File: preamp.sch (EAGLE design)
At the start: 30 parts, among them IC1 INA2141U, IC2 INA2141U, IC3 INA2141U

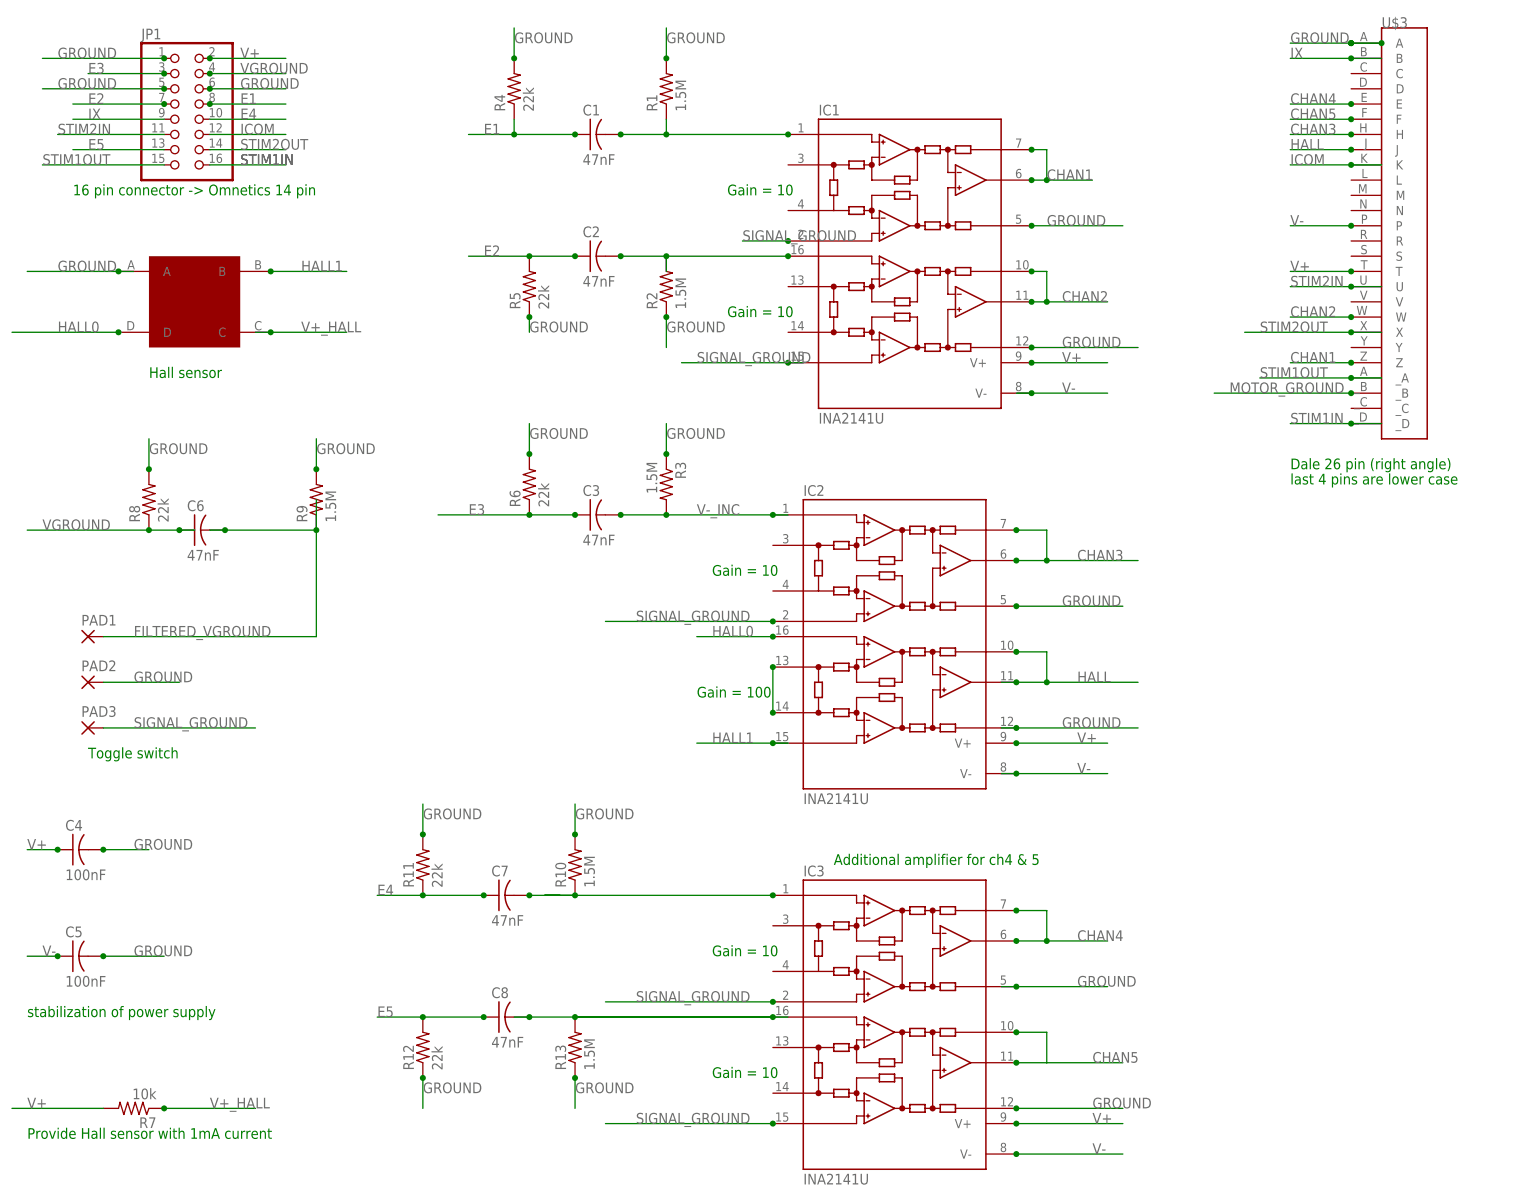
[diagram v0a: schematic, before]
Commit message: Preamp - Removed VGROUND
SIGNAL_GROUND net changed to GROUND
Removed filter circuitry for VGROUND
Removed toggle switch between GROUND and FILTERED_VGND for
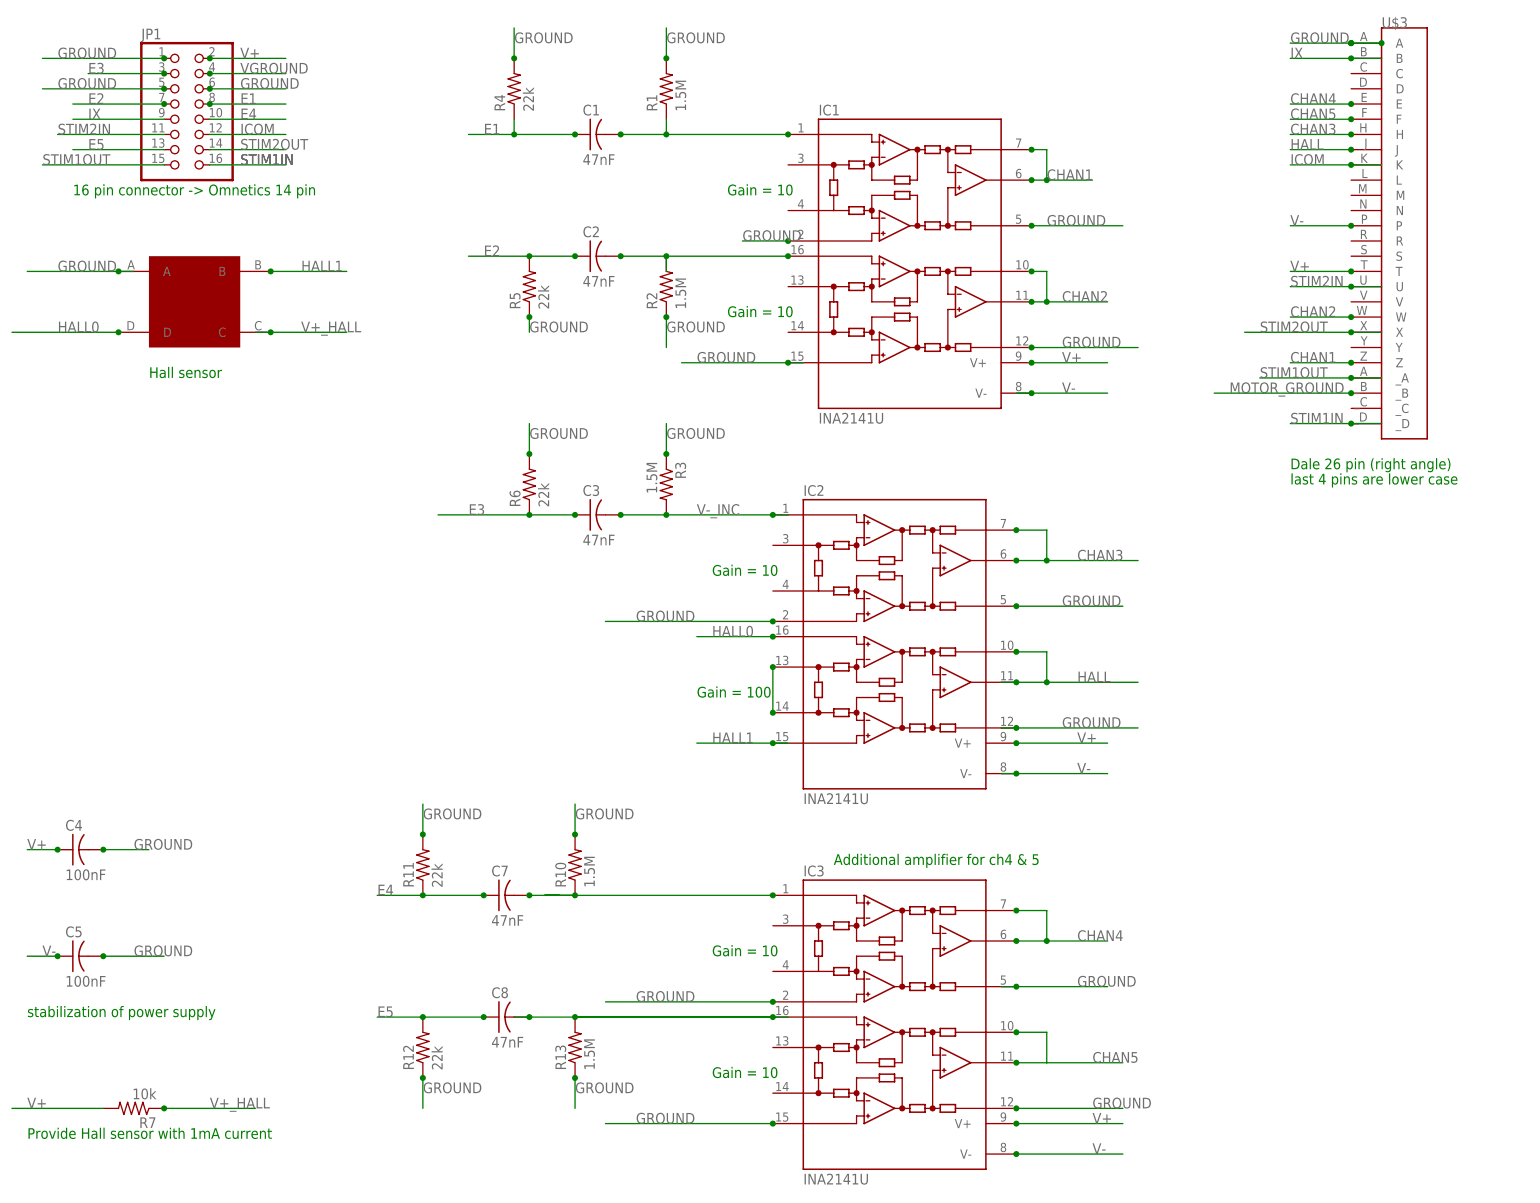
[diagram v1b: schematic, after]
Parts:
- removed C6: 47nF, elm:C0805ELM
- removed PAD1, PAD2, PAD3: (no value), wirepad:SMD2
- removed R8: 22k, elm:R0805ELM
- removed R9: 1.5M, elm:R0805ELM
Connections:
- removed net FILTERED_VGROUND: C6.2, PAD1.P, R9.1
- removed net SIGNAL_GROUND: IC1.INA+, IC1.INB+, IC2.INA+, IC3.INA+, IC3.INB+, PAD3.P
- net GROUND: now also IC1.INA+, IC1.INB+, IC2.INA+, IC3.INA+, IC3.INB+; no longer PAD2.P, R8.2, R9.2
- net VGROUND: no longer C6.1, R8.1
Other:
- note removed: "Toggle switch"
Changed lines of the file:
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@@
 <?xml version="1.0" encoding="utf-8"?>
 <!DOCTYPE eagle SYSTEM "eagle.dtd">
-<eagle version="6.2">
+<eagle version="7.5.0">
 <drawing>
 <settings>
@@
 <part name="C4" library="elm" deviceset="C0805ELM" device="" value="100nF"/>
 <part name="C5" library="elm" deviceset="C0805ELM" device="" value="100nF"/>
-<part name="R8" library="elm" deviceset="R0805ELM" device="" value="22k"/>
-<part name="C6" library="elm" deviceset="C0805ELM" device="" value="47nF"/>
-<part name="R9" library="elm" deviceset="R0805ELM" device="" value="1.5M"/>
 <part name="U$3" library="elm" deviceset="MMD1P22G-26-M101" device=""/>
 <part name="JP1" library="pinhead" deviceset="PINHD-2X8" device=""/>
 <part name="U$2" library="elm" deviceset="HALL_ON_SIDE" device="" value="HALL"/>
-<part name="PAD1" library="wirepad" deviceset="SMD2" device=""/>
-<part name="PAD2" library="wirepad" deviceset="SMD2" device=""/>
-<part name="PAD3" library="wirepad" deviceset="SMD2" device=""/>
 <part name="IC3" library="burr-brown" deviceset="INA2141" device="U"/>
 <part name="C7" library="elm" deviceset="C0805ELM" device="" value="47nF"/>
@@
 <text x="-106.68" y="63.5" size="1.778" layer="91">Gain = 10</text>
 <text x="-220.98" y="33.02" size="1.778" layer="91">Provide Hall sensor with 1mA current</text>
-<text x="-210.82" y="96.52" size="1.778" layer="91">Toggle switch</text>
 <text x="-10.16" y="142.24" size="1.778" layer="91">last 4 pins are lower case</text>
 <text x="-213.36" y="190.5" size="1.778" layer="91">16 pin connector -&gt; Omnetics 14 pin</text>
@@
 <instance part="C4" gate="G$1" x="-213.36" y="81.28"/>
 <instance part="C5" gate="G$1" x="-213.36" y="63.5"/>
-<instance part="R8" gate="G$1" x="-200.66" y="139.7" rot="R90"/>
-<instance part="C6" gate="G$1" x="-193.04" y="134.62"/>
-<instance part="R9" gate="G$1" x="-172.72" y="139.7" rot="R90"/>
 <instance part="U$3" gate="G$1" x="10.16" y="187.96"/>
 <instance part="JP1" gate="A" x="-195.58" y="205.74"/>
 <instance part="U$2" gate="G$1" x="-193.04" y="172.72"/>
-<instance part="PAD1" gate="1" x="-210.82" y="116.84"/>
-<instance part="PAD2" gate="1" x="-210.82" y="109.22"/>
-<instance part="PAD3" gate="1" x="-210.82" y="101.6"/>
 <instance part="IC3" gate="G$1" x="-73.66" y="53.34"/>
 <instance part="C7" gate="G$1" x="-142.24" y="73.66"/>
@@
 </segment>
 <segment>
-<wire x1="-208.28" y1="109.22" x2="-195.58" y2="109.22" width="0.1524" layer="91"/>
-<label x="-203.2" y="109.22" size="1.778" layer="95"/>
-<pinref part="PAD2" gate="1" pin="P"/>
-</segment>
-<segment>
-<pinref part="R8" gate="G$1" pin="2"/>
-<wire x1="-200.66" y1="144.78" x2="-200.66" y2="149.86" width="0.1524" layer="91"/>
-<label x="-200.66" y="147.32" size="1.778" layer="95"/>
-<junction x="-200.66" y="144.78"/>
-</segment>
-<segment>
-<pinref part="R9" gate="G$1" pin="2"/>
-<wire x1="-172.72" y1="144.78" x2="-172.72" y2="149.86" width="0.1524" layer="91"/>
-<label x="-172.72" y="147.32" size="1.778" layer="95"/>
-<junction x="-172.72" y="144.78"/>
-</segment>
-<segment>
 <label x="-10.16" y="215.9" size="1.778" layer="95"/>
 <pinref part="U$3" gate="G$1" pin="A"/>
@@
 <label x="-129.54" y="86.36" size="1.778" layer="95"/>
 </segment>
-</net>
-<net name="V+" class="0">
-<segment>
-<pinref part="IC1" gate="G$1" pin="V+"/>
-<wire x1="-53.34" y1="162.56" x2="-40.64" y2="162.56" width="0.1524" layer="91"/>
-<label x="-48.26" y="162.56" size="1.778" layer="95"/>
-<junction x="-53.34" y="162.56"/>
-</segment>
-<segment>
-<pinref part="IC2" gate="G$1" pin="V+"/>
-<wire x1="-55.88" y1="99.06" x2="-40.64" y2="99.06" width="0.1524" layer="91"/>
-<label x="-45.72" y="99.06" size="1.778" layer="95"/>
-<junction x="-55.88" y="99.06"/>
-</segment>
-<segment>
-<wire x1="-223.52" y1="38.1" x2="-208.28" y2="38.1" width="0.1524" layer="91"/>
-<pinref part="R7" gate="G$1" pin="2"/>
-<label x="-220.98" y="38.1" size="1.778" layer="95"/>
-</segment>
-<segment>
-<pinref part="C4" gate="G$1" pin="1"/>
-<wire x1="-215.9" y1="81.28" x2="-220.98" y2="81.28" width="0.1524" layer="91"/>
-<label x="-220.98" y="81.28" size="1.778" layer="95"/>
-<junction x="-215.9" y="81.28"/>
-</segment>
-<segment>
-<label x="-10.16" y="177.8" size="1.778" layer="95"/>
-<pinref part="U$3" gate="G$1" pin="T"/>
-<junction x="0" y="177.8"/>
-<wire x1="0" y1="177.8" x2="-10.16" y2="177.8" width="0.1524" layer="91"/>
-</segment>
-<segment>
-<pinref part="JP1" gate="A" pin="2"/>
-<wire x1="-190.5" y1="213.36" x2="-177.8" y2="213.36" width="0.1524" layer="91"/>
-<junction x="-190.5" y="213.36"/>
-<label x="-185.42" y="213.36" size="1.778" layer="95"/>
-</segment>
-<segment>
-<pinref part="IC3" gate="G$1" pin="V+"/>
-<wire x1="-55.88" y1="35.56" x2="-38.1" y2="35.56" width="0.1524" layer="91"/>
-<label x="-43.18" y="35.56" size="1.778" layer="95"/>
-<junction x="-55.88" y="35.56"/>
-</segment>
-</net>
-<net name="SIGNAL_GROUND" class="0">
 <segment>
 <pinref part="IC1" gate="G$1" pin="INA+"/>
@@
 <label x="-101.6" y="182.88" size="1.778" layer="95"/>
 <junction x="-93.98" y="182.88"/>
-</segment>
-<segment>
-<wire x1="-208.28" y1="101.6" x2="-182.88" y2="101.6" width="0.1524" layer="91"/>
-<label x="-203.2" y="101.6" size="1.778" layer="95"/>
-<pinref part="PAD3" gate="1" pin="P"/>
 </segment>
 <segment>
@@
 </segment>
 </net>
+<net name="V+" class="0">
+<segment>
+<pinref part="IC1" gate="G$1" pin="V+"/>
+<wire x1="-53.34" y1="162.56" x2="-40.64" y2="162.56" width="0.1524" layer="91"/>
+<label x="-48.26" y="162.56" size="1.778" layer="95"/>
+<junction x="-53.34" y="162.56"/>
+</segment>
+<segment>
+<pinref part="IC2" gate="G$1" pin="V+"/>
+<wire x1="-55.88" y1="99.06" x2="-40.64" y2="99.06" width="0.1524" layer="91"/>
+<label x="-45.72" y="99.06" size="1.778" layer="95"/>
+<junction x="-55.88" y="99.06"/>
+</segment>
+<segment>
+<wire x1="-223.52" y1="38.1" x2="-208.28" y2="38.1" width="0.1524" layer="91"/>
+<pinref part="R7" gate="G$1" pin="2"/>
+<label x="-220.98" y="38.1" size="1.778" layer="95"/>
+</segment>
+<segment>
+<pinref part="C4" gate="G$1" pin="1"/>
+<wire x1="-215.9" y1="81.28" x2="-220.98" y2="81.28" width="0.1524" layer="91"/>
+<label x="-220.98" y="81.28" size="1.778" layer="95"/>
+<junction x="-215.9" y="81.28"/>
+</segment>
+<segment>
+<label x="-10.16" y="177.8" size="1.778" layer="95"/>
+<pinref part="U$3" gate="G$1" pin="T"/>
+<junction x="0" y="177.8"/>
+<wire x1="0" y1="177.8" x2="-10.16" y2="177.8" width="0.1524" layer="91"/>
+</segment>
+<segment>
+<pinref part="JP1" gate="A" pin="2"/>
+<wire x1="-190.5" y1="213.36" x2="-177.8" y2="213.36" width="0.1524" layer="91"/>
+<junction x="-190.5" y="213.36"/>
+<label x="-185.42" y="213.36" size="1.778" layer="95"/>
+</segment>
+<segment>
+<pinref part="IC3" gate="G$1" pin="V+"/>
+<wire x1="-55.88" y1="35.56" x2="-38.1" y2="35.56" width="0.1524" layer="91"/>
+<label x="-43.18" y="35.56" size="1.778" layer="95"/>
+<junction x="-55.88" y="35.56"/>
+</segment>
+</net>
 <net name="VGROUND" class="0">
-<segment>
-<pinref part="R8" gate="G$1" pin="1"/>
-<wire x1="-200.66" y1="134.62" x2="-195.58" y2="134.62" width="0.1524" layer="91"/>
-<pinref part="C6" gate="G$1" pin="1"/>
-<wire x1="-195.58" y1="134.62" x2="-193.04" y2="134.62" width="0.1524" layer="91"/>
-<junction x="-195.58" y="134.62"/>
-<wire x1="-200.66" y1="134.62" x2="-220.98" y2="134.62" width="0.1524" layer="91"/>
-<junction x="-200.66" y="134.62"/>
-<label x="-218.44" y="134.62" size="1.778" layer="95"/>
-</segment>
 <segment>
 <pinref part="JP1" gate="A" pin="4"/>
@@
 </segment>
 </net>
-<net name="FILTERED_VGROUND" class="0">
-<segment>
-<wire x1="-190.5" y1="134.62" x2="-187.96" y2="134.62" width="0.1524" layer="91"/>
-<wire x1="-187.96" y1="134.62" x2="-172.72" y2="134.62" width="0.1524" layer="91"/>
-<wire x1="-172.72" y1="134.62" x2="-172.72" y2="116.84" width="0.1524" layer="91"/>
-<wire x1="-172.72" y1="116.84" x2="-208.28" y2="116.84" width="0.1524" layer="91"/>
-<label x="-203.2" y="116.84" size="1.778" layer="95"/>
-<pinref part="C6" gate="G$1" pin="2"/>
-<junction x="-187.96" y="134.62"/>
-<pinref part="PAD1" gate="1" pin="P"/>
-<pinref part="R9" gate="G$1" pin="1"/>
-<wire x1="-172.72" y1="139.7" x2="-172.72" y2="134.62" width="0.1524" layer="91"/>
-<junction x="-172.72" y="134.62"/>
-</segment>
-</net>

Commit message: Changed JP1 pinout to match drive
Stim 1 In > DGND
Stim 1 Out > SCL
IX > IX
E4 > SDA
VGND > E3
E5 > E1
E3 > E4
GROUND > E2
E2 > ICOM
ICOM > V+
E1 > GROUND
V+ > V-
STIM2 stays the same
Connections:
- net STIM1OUT renamed SCL
- removed net STIM1IN: JP1.16, U$3._D
- removed net VGROUND: JP1.4
- new net DGND: JP1.16, U$3._C
- new net SDA: JP1.10, U$3._D
- net CHAN1: now also IC3.SENSEA, IC3.VOA; no longer IC1.SENSEA, IC1.VOA
- net CHAN4: now also IC1.SENSEA, IC1.VOA; no longer IC3.SENSEA, IC3.VOA
- net E1: now also C7.1, JP1.13, R11.1; no longer C1.1, JP1.8, R4.1
- net E2: now also JP1.1, JP1.5, JP1.6; no longer JP1.7
- net E3: now also JP1.4; no longer JP1.3
- net E4: now also C1.1, JP1.3, R4.1; no longer C7.1, JP1.10, R11.1
- net E5: no longer JP1.13
- net GROUND: now also JP1.8; no longer JP1.1, JP1.5, JP1.6
- net ICOM: now also JP1.7; no longer JP1.12
- net V+: now also JP1.12; no longer JP1.2
- net V-: now also JP1.2
